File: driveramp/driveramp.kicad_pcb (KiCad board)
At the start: 4 copper layers, 17 parts, among them J1 SMA, J2 SMA, Q1 MRFE6VS25L

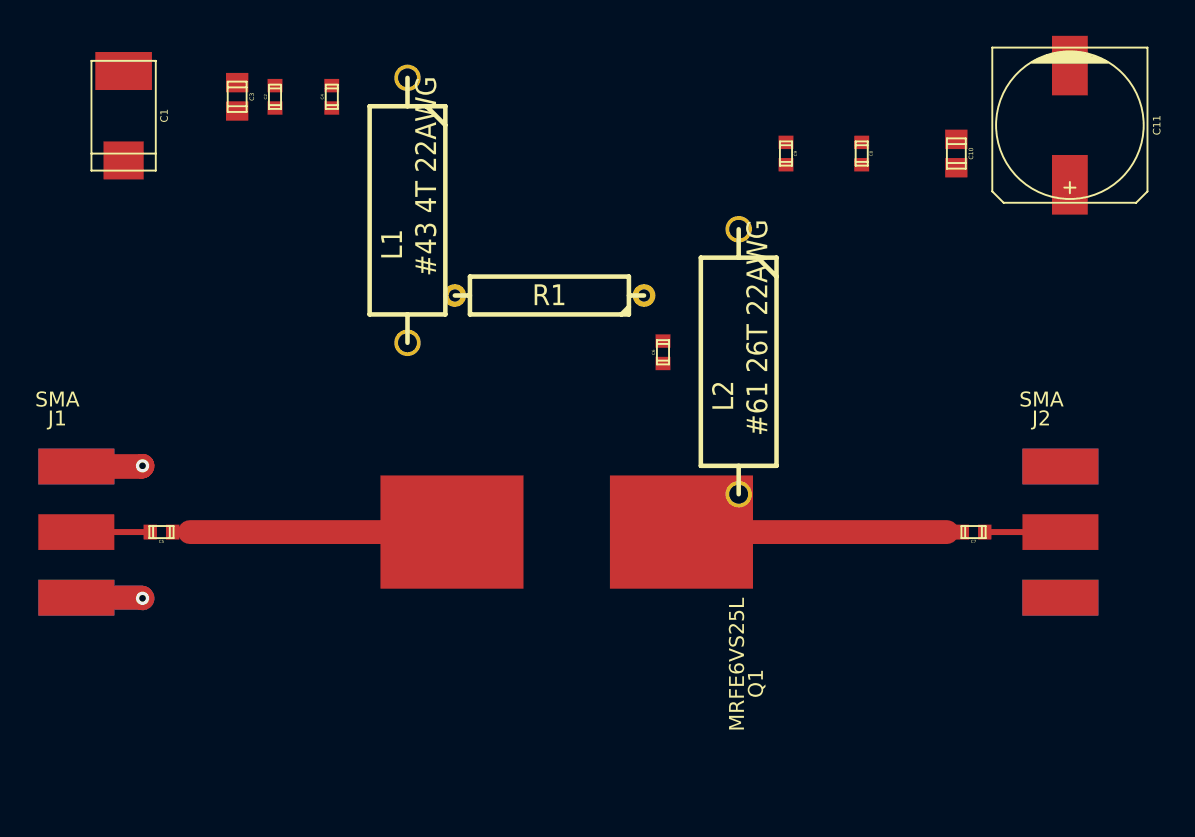
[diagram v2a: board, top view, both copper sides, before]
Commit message: layout work on driver amp
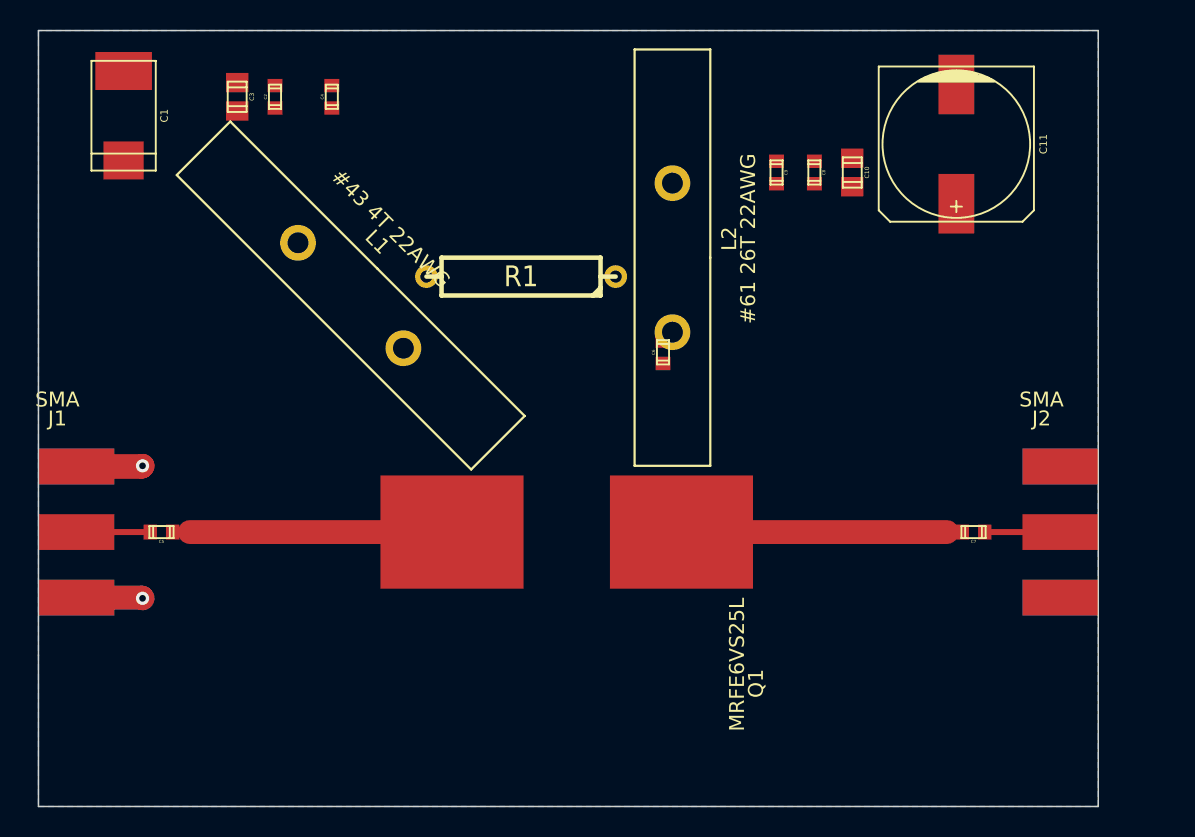
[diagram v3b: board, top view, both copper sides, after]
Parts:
- L1, L2: footprint R7 -> toroid
- moved L2 8.28 mm to (137.8, 63.5)
- moved C11 7.73 mm to (156.8, 55.9)
- moved C10 7.10 mm to (149.9, 57.8)
- moved L1 6.87 mm to (116.2, 66.0), turned to 315 degrees
- moved C8 3.42 mm to (147.3, 57.8)
- moved R1 2.29 mm to (127.6, 64.8)
- moved C9 1.42 mm to (144.8, 57.8)
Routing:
- added copper zone on B.Cu, net GND
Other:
- board outline added: 71.1 x 52.1 mm
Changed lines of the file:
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@@
   (general
     (links 32)
-    (no_connects 25)
-    (area 90.13962 30.966827 175.86188 97.235555)
+    (no_connects 23)
+    (area 93.978334 47.476827 171.41688 100.380001)
     (thickness 1.6)
-    (drawings 0)
+    (drawings 5)
     (tracks 17)
     (zones 0)
@@
     (2 Inner2.Cu power)
     (1 Inner1.Cu power)
-    (0 B.Cu signal)
+    (0 B.Cu signal hide)
     (16 B.Adhes user)
     (17 F.Adhes user)
@@
   )
   (setup
-    (last_trace_width 0.4)
+    (last_trace_width 0.254)
     (user_trace_width 0.254)
     (user_trace_width 0.4)
@@
     (mod_text_size 1 1)
     (mod_text_width 0.15)
-    (pad_size 5 2.4)
-    (pad_drill 0)
+    (pad_size 2.4 2.4)
+    (pad_drill 1.4)
     (pad_to_mask_clearance 0)
     (aux_axis_origin 0 0)
@@
     )
   )
-  (module R7 (layer F.Cu)
-    (at 120.015 60.325 270)
-    (descr "Resitance 7 pas")
-    (tags R)
-    (autoplace_cost180 10)
-    (fp_text reference L1 (at 2.286 1.016 270) (layer F.SilkS)
-      (effects (font (size 1.397 1.27) (thickness 0.2032)))
-    )
-    (fp_text value "#43 4T 22AWG" (at -2.286 -1.27 270) (layer F.SilkS)
-      (effects (font (size 1.397 1.27) (thickness 0.2032)))
-    )
-    (fp_line (start -8.89 0) (end -8.89 0) (layer F.SilkS) (width 0.3048))
-    (fp_line (start -8.89 0) (end -8.89 0) (layer F.SilkS) (width 0.3048))
-    (fp_line (start 6.985 0) (end 8.89 0) (layer F.SilkS) (width 0.3048))
-    (fp_line (start 8.89 0) (end 8.89 0) (layer F.SilkS) (width 0.3048))
-    (fp_line (start 6.985 2.54) (end -6.985 2.54) (layer F.SilkS) (width 0.3048))
-    (fp_line (start -6.985 -2.54) (end 6.985 -2.54) (layer F.SilkS) (width 0.3048))
-    (fp_line (start -6.985 -1.27) (end -5.715 -2.54) (layer F.SilkS) (width 0.3048))
-    (fp_line (start 6.985 -2.54) (end 6.985 2.54) (layer F.SilkS) (width 0.3048))
-    (fp_line (start -6.985 -2.54) (end -6.985 2.54) (layer F.SilkS) (width 0.3048))
-    (fp_line (start -8.89 0) (end -6.985 0) (layer F.SilkS) (width 0.3048))
-    (pad 1 thru_hole circle (at -8.89 0 270) (size 1.778 1.778) (drill 1.27)
-      (layers *.Cu *.Mask F.SilkS)
-      (net 1 /vbias)
-    )
-    (pad 2 thru_hole circle (at 8.89 0 270) (size 1.778 1.778) (drill 1.27)
-      (layers *.Cu *.Mask F.SilkS)
-      (net 6 N-000003)
-    )
-    (model discret/resistor.wrl
-      (at (xyz 0 0 0))
-      (scale (xyz 0.7 0.7 0.7))
-      (rotate (xyz 0 0 0))
-    )
-  )
-  (module R7 (layer F.Cu)
-    (at 142.24 70.485 270)
-    (descr "Resitance 7 pas")
-    (tags R)
-    (autoplace_cost180 10)
-    (fp_text reference L2 (at 2.286 1.016 270) (layer F.SilkS)
-      (effects (font (size 1.397 1.27) (thickness 0.2032)))
-    )
-    (fp_text value "#61 26T 22AWG" (at -2.286 -1.27 270) (layer F.SilkS)
-      (effects (font (size 1.397 1.27) (thickness 0.2032)))
-    )
-    (fp_line (start -8.89 0) (end -8.89 0) (layer F.SilkS) (width 0.3048))
-    (fp_line (start -8.89 0) (end -8.89 0) (layer F.SilkS) (width 0.3048))
-    (fp_line (start 6.985 0) (end 8.89 0) (layer F.SilkS) (width 0.3048))
-    (fp_line (start 8.89 0) (end 8.89 0) (layer F.SilkS) (width 0.3048))
-    (fp_line (start 6.985 2.54) (end -6.985 2.54) (layer F.SilkS) (width 0.3048))
-    (fp_line (start -6.985 -2.54) (end 6.985 -2.54) (layer F.SilkS) (width 0.3048))
-    (fp_line (start -6.985 -1.27) (end -5.715 -2.54) (layer F.SilkS) (width 0.3048))
-    (fp_line (start 6.985 -2.54) (end 6.985 2.54) (layer F.SilkS) (width 0.3048))
-    (fp_line (start -6.985 -2.54) (end -6.985 2.54) (layer F.SilkS) (width 0.3048))
-    (fp_line (start -8.89 0) (end -6.985 0) (layer F.SilkS) (width 0.3048))
-    (pad 1 thru_hole circle (at -8.89 0 270) (size 1.778 1.778) (drill 1.27)
-      (layers *.Cu *.Mask F.SilkS)
-      (net 2 /vsupply)
-    )
-    (pad 2 thru_hole circle (at 8.89 0 270) (size 1.778 1.778) (drill 1.27)
-      (layers *.Cu *.Mask F.SilkS)
-      (net 7 N-000007)
-    )
-    (model discret/resistor.wrl
-      (at (xyz 0 0 0))
-      (scale (xyz 0.7 0.7 0.7))
-      (rotate (xyz 0 0 0))
-    )
-  )
   (module R5 (layer F.Cu)
-    (at 129.54 66.04 180)
+    (at 127.635 64.77 180)
     (descr "Resistance 5 pas")
     (tags R)
@@
   )
   (module c_elec_10x10 (layer F.Cu)
-    (at 164.465 54.61 270)
+    (at 156.845 55.88 270)
     (descr "SMT capacitor, aluminium electrolytic, 10x10")
     (fp_text reference C11 (at 0 -5.842 270) (layer F.SilkS)
@@
   )
   (module c_0805 (layer F.Cu)
-    (at 156.845 56.515 270)
+    (at 149.86 57.785 270)
     (descr "SMT capacitor, 0805")
     (fp_text reference C10 (at 0 -0.9906 270) (layer F.SilkS)
@@
   )
   (module c_0603 (layer F.Cu)
-    (at 150.495 56.515 270)
+    (at 147.32 57.785 270)
     (descr "SMT capacitor, 0603")
     (fp_text reference C8 (at 0 -0.635 270) (layer F.SilkS)
@@
   )
   (module c_0603 (layer F.Cu)
-    (at 145.415 56.515 270)
+    (at 144.78 57.785 270)
     (descr "SMT capacitor, 0603")
     (fp_text reference C9 (at 0 -0.635 270) (layer F.SilkS)
@@
     )
   )
+  (module toroid (layer F.Cu)
+    (at 116.205 66.04 315)
+    (fp_text reference L1 (at -1.27 -3.81 315) (layer F.SilkS)
+      (effects (font (size 1 1) (thickness 0.15)))
+    )
+    (fp_text value "#43 4T 22AWG" (at -1.27 -5.08 315) (layer F.SilkS)
+      (effects (font (size 1 1) (thickness 0.15)))
+    )
+    (fp_line (start 0 -2.54) (end -13.97 -2.54) (layer F.SilkS) (width 0.15))
+    (fp_line (start -13.97 -2.54) (end -13.97 2.54) (layer F.SilkS) (width 0.15))
+    (fp_line (start -13.97 2.54) (end 13.97 2.54) (layer F.SilkS) (width 0.15))
+    (fp_line (start 13.97 2.54) (end 13.97 -2.54) (layer F.SilkS) (width 0.15))
+    (fp_line (start 13.97 -2.54) (end 0 -2.54) (layer F.SilkS) (width 0.15))
+    (pad 2 thru_hole circle (at 5 0 315) (size 2.4 2.4) (drill 1.4)
+      (layers *.Cu *.Mask F.SilkS)
+      (net 6 N-000003)
+    )
+    (pad 1 thru_hole circle (at -5 0 315) (size 2.4 2.4) (drill 1.4)
+      (layers *.Cu *.Mask F.SilkS)
+      (net 1 /vbias)
+    )
+  )
+  (module toroid (layer F.Cu)
+    (at 137.795 63.5 270)
+    (fp_text reference L2 (at -1.27 -3.81 270) (layer F.SilkS)
+      (effects (font (size 1 1) (thickness 0.15)))
+    )
+    (fp_text value "#61 26T 22AWG" (at -1.27 -5.08 270) (layer F.SilkS)
+      (effects (font (size 1 1) (thickness 0.15)))
+    )
+    (fp_line (start 0 -2.54) (end -13.97 -2.54) (layer F.SilkS) (width 0.15))
+    (fp_line (start -13.97 -2.54) (end -13.97 2.54) (layer F.SilkS) (width 0.15))
+    (fp_line (start -13.97 2.54) (end 13.97 2.54) (layer F.SilkS) (width 0.15))
+    (fp_line (start 13.97 2.54) (end 13.97 -2.54) (layer F.SilkS) (width 0.15))
+    (fp_line (start 13.97 -2.54) (end 0 -2.54) (layer F.SilkS) (width 0.15))
+    (pad 2 thru_hole circle (at 5 0 270) (size 2.4 2.4) (drill 1.4)
+      (layers *.Cu *.Mask F.SilkS)
+      (net 7 N-000007)
+    )
+    (pad 1 thru_hole circle (at -5 0 270) (size 2.4 2.4) (drill 1.4)
+      (layers *.Cu *.Mask F.SilkS)
+      (net 2 /vsupply)
+    )
+  )
+  (gr_line (start 95.25 48.26) (end 166.37 48.26) (angle 90) (layer Edge.Cuts) (width 0.1))
+  (gr_line (start 166.37 100.33) (end 166.37 48.26) (angle 90) (layer Edge.Cuts) (width 0.1))
+  (gr_line (start 95.25 100.33) (end 166.37 100.33) (angle 90) (layer Edge.Cuts) (width 0.1))
+  (gr_line (start 95.25 90.17) (end 95.25 100.33) (angle 90) (layer Edge.Cuts) (width 0.1))
+  (gr_line (start 95.25 90.17) (end 95.25 48.26) (angle 90) (layer Edge.Cuts) (width 0.1))
   (segment (start 97.79 77.515) (end 102.19 77.515) (width 1.6) (layer B.Cu) (net 3))
   (segment (start 97.79 77.515) (end 102.19 77.515) (width 1.6) (layer F.Cu) (net 3))
@@
   (segment (start 104.25684 81.915) (end 105.41 81.915) (width 0.4) (layer F.Cu) (net 8))
   (segment (start 105.41 81.915) (end 123 81.915) (width 1.6) (layer F.Cu) (net 8))
+  (zone (net 3) (net_name GND) (layer B.Cu) (hatch edge 0.508)
+    (connect_pads (clearance 0.508))
+    (min_thickness 0.254)
+    (fill (arc_segments 16) (thermal_gap 0.508) (thermal_bridge_width 0.508))
+    (polygon
+      (pts
+        (xy 95.25 48.26) (xy 95.25 100.33) (xy 166.37 100.33) (xy 166.37 48.26)
+      )
+    )
+  )
 )

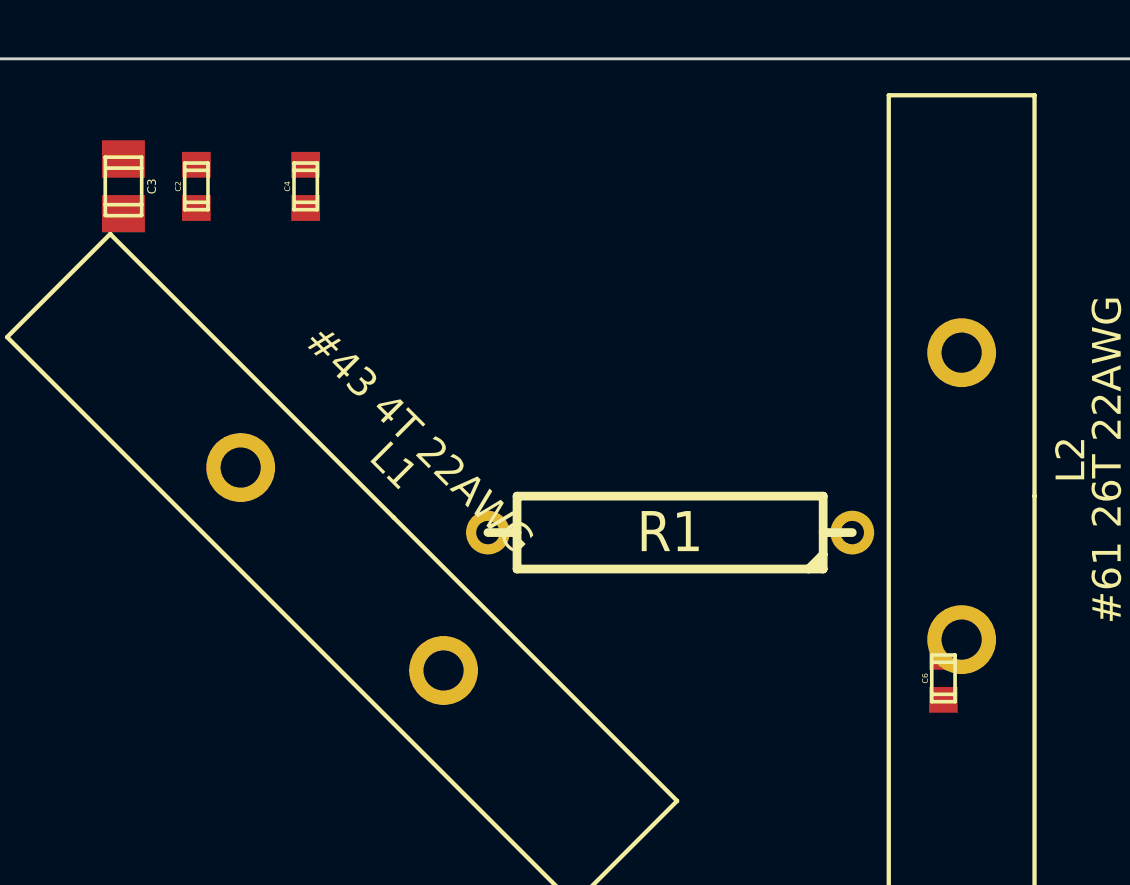
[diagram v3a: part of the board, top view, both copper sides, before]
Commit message: driver amp layout
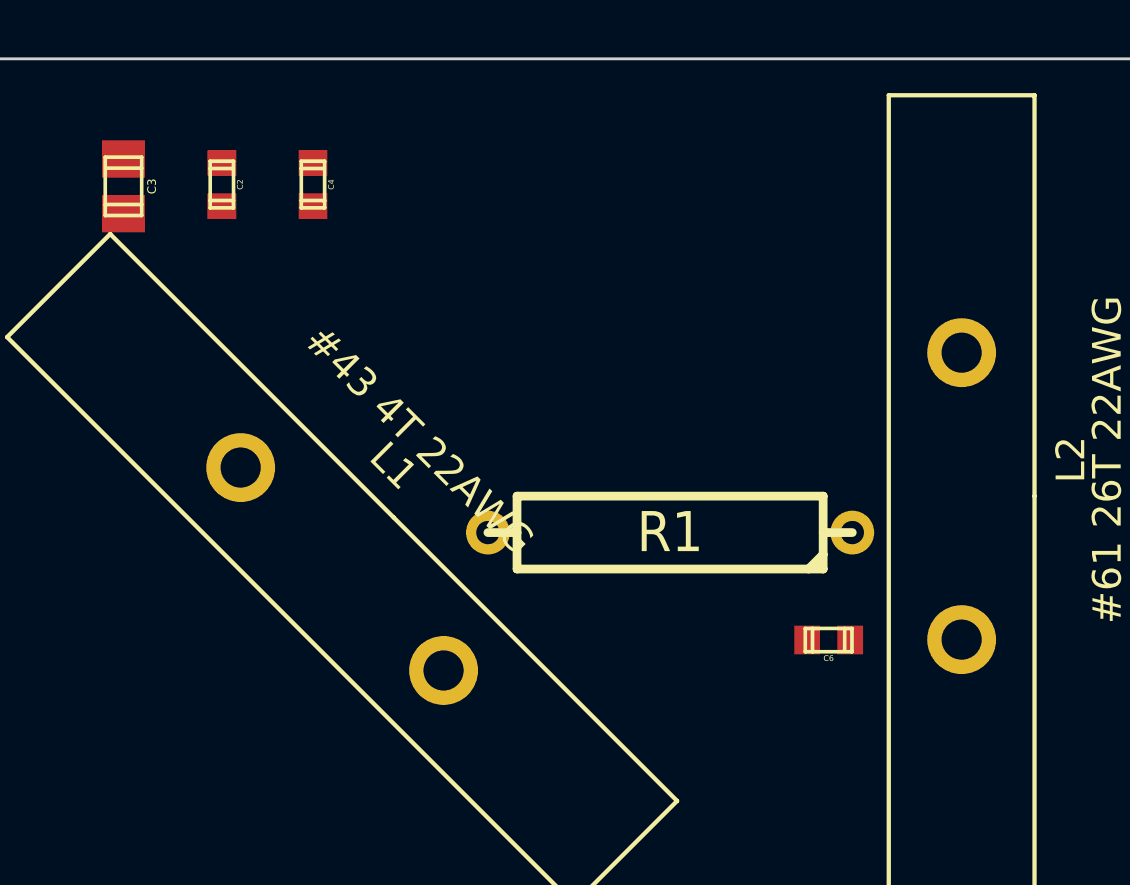
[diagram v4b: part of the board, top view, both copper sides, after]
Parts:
- moved C6 4.22 mm to (133.2, 68.5), turned to 180 degrees
- moved C2 0.89 mm to (112.0, 52.6), turned to 270 degrees
- moved C4 0.26 mm to (115.2, 52.6), turned to 270 degrees
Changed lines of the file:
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@@
     (links 32)
     (no_connects 23)
-    (area 93.978334 47.476827 171.41688 100.380001)
+    (area 93.978334 47.887133 167.448245 100.380001)
     (thickness 1.6)
     (drawings 5)
@@
   )
   (module c_0603 (layer F.Cu)
-    (at 111.125 52.705 90)
+    (at 112.014 52.6415 270)
     (descr "SMT capacitor, 0603")
-    (fp_text reference C2 (at 0 -0.635 90) (layer F.SilkS)
-      (effects (font (size 0.20066 0.20066) (thickness 0.04064)))
-    )
-    (fp_text value "100nF 50V" (at 0 0.635 90) (layer F.SilkS) hide
+    (fp_text reference C2 (at 0 -0.635 270) (layer F.SilkS)
+      (effects (font (size 0.20066 0.20066) (thickness 0.04064)))
+    )
+    (fp_text value "100nF 50V" (at 0 0.635 270) (layer F.SilkS) hide
       (effects (font (size 0.20066 0.20066) (thickness 0.04064)))
     )
@@
     (fp_line (start 0.8128 0.4064) (end -0.8128 0.4064) (layer F.SilkS) (width 0.127))
     (fp_line (start -0.8128 0.4064) (end -0.8128 -0.4064) (layer F.SilkS) (width 0.127))
-    (pad 1 smd rect (at 0.75184 0 90) (size 0.89916 1.00076)
+    (pad 1 smd rect (at 0.75184 0 270) (size 0.89916 1.00076)
       (layers F.Cu F.Paste F.Mask)
       (net 1 /vbias)
     )
-    (pad 2 smd rect (at -0.75184 0 90) (size 0.89916 1.00076)
+    (pad 2 smd rect (at -0.75184 0 270) (size 0.89916 1.00076)
       (layers F.Cu F.Paste F.Mask)
       (net 3 GND)
@@
   )
   (module c_0603 (layer F.Cu)
-    (at 114.935 52.705 90)
+    (at 115.189 52.6415 270)
     (descr "SMT capacitor, 0603")
-    (fp_text reference C4 (at 0 -0.635 90) (layer F.SilkS)
-      (effects (font (size 0.20066 0.20066) (thickness 0.04064)))
-    )
-    (fp_text value 10nF (at 0 0.635 90) (layer F.SilkS) hide
+    (fp_text reference C4 (at 0 -0.635 270) (layer F.SilkS)
+      (effects (font (size 0.20066 0.20066) (thickness 0.04064)))
+    )
+    (fp_text value 10nF (at 0 0.635 270) (layer F.SilkS) hide
       (effects (font (size 0.20066 0.20066) (thickness 0.04064)))
     )
@@
     (fp_line (start 0.8128 0.4064) (end -0.8128 0.4064) (layer F.SilkS) (width 0.127))
     (fp_line (start -0.8128 0.4064) (end -0.8128 -0.4064) (layer F.SilkS) (width 0.127))
-    (pad 1 smd rect (at 0.75184 0 90) (size 0.89916 1.00076)
+    (pad 1 smd rect (at 0.75184 0 270) (size 0.89916 1.00076)
       (layers F.Cu F.Paste F.Mask)
       (net 1 /vbias)
     )
-    (pad 2 smd rect (at -0.75184 0 90) (size 0.89916 1.00076)
+    (pad 2 smd rect (at -0.75184 0 270) (size 0.89916 1.00076)
       (layers F.Cu F.Paste F.Mask)
       (net 3 GND)
@@
   )
   (module c_0603 (layer F.Cu)
-    (at 137.16 69.85 90)
+    (at 133.1595 68.5165 180)
     (descr "SMT capacitor, 0603")
-    (fp_text reference C6 (at 0 -0.635 90) (layer F.SilkS)
-      (effects (font (size 0.20066 0.20066) (thickness 0.04064)))
-    )
-    (fp_text value 20nF (at 0 0.635 90) (layer F.SilkS) hide
+    (fp_text reference C6 (at 0 -0.635 180) (layer F.SilkS)
+      (effects (font (size 0.20066 0.20066) (thickness 0.04064)))
+    )
+    (fp_text value 20nF (at 0 0.635 180) (layer F.SilkS) hide
       (effects (font (size 0.20066 0.20066) (thickness 0.04064)))
     )
@@
     (fp_line (start 0.8128 0.4064) (end -0.8128 0.4064) (layer F.SilkS) (width 0.127))
     (fp_line (start -0.8128 0.4064) (end -0.8128 -0.4064) (layer F.SilkS) (width 0.127))
-    (pad 1 smd rect (at 0.75184 0 90) (size 0.89916 1.00076)
+    (pad 1 smd rect (at 0.75184 0 180) (size 0.89916 1.00076)
       (layers F.Cu F.Paste F.Mask)
       (net 9 N-000009)
     )
-    (pad 2 smd rect (at -0.75184 0 90) (size 0.89916 1.00076)
+    (pad 2 smd rect (at -0.75184 0 180) (size 0.89916 1.00076)
       (layers F.Cu F.Paste F.Mask)
       (net 7 N-000007)

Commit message: r0 driver amp breakout ready for manufacturing:
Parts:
- added P1: CONN_2, connect:SIL-2, F.Cu at (118.6, 51.8)
- added P2: CONN_2, connect:SIL-2, F.Cu at (145.3, 51.6)
- L1: value #43 4T 22AWG -> #43 4T 22AWG .01mH
- L2: value #61 26T 22AWG -> #61 26T 22AWG, .04mH
- moved L2 7.75 mm to (140.7, 70.7)
- moved C6 4.97 mm to (135.6, 72.9), turned to 90 degrees
- moved R1 3.39 mm to (129.2, 67.8)
- moved C4 2.48 mm to (113.3, 51.1)
- moved C3 1.94 mm to (109.0, 50.8)
- moved C2 1.76 mm to (111.3, 51.1)
- moved C1 1.20 mm to (99.8, 54.4), turned to 90 degrees
- moved L1 1.17 mm to (115.1, 65.8)
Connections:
- C5 pad 2: N-000008 -> Net-(C5-Pad2)
- L1 pad 2: N-000003 -> Net-(C5-Pad2)
- Q1 pad G: N-000008 -> Net-(C5-Pad2)
- R1 pad 2: N-000003 -> Net-(C5-Pad2)
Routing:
- net Net-(C5-Pad2): track 0.00 -> 38.0 mm
- net /vsupply: track 0.00 -> 37.5 mm
- net GND: track 22.3 -> 58.5 mm, vias 2 -> 12
- net /vbias: track 0.00 -> 32.8 mm
- net Net-(C6-Pad2): track 18.8 -> 39.4 mm
- net N-000008: track 18.7 -> 0.00 mm
- net Net-(C6-Pad1): track 0.00 -> 4.36 mm
- net Net-(C5-Pad1): track 4.96 -> 5.61 mm
- net Net-(C7-Pad2): track 5.08 -> 5.71 mm
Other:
- board text added: "jon klein jtklein@alaska.edu driver amp breakout"
- board text added: "this side down"
- board text added: "vbias"
- board text added: "vdd"

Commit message: added barrel connector to driver amp, finished medium power T/R layout
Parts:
- removed P1: CONN_2, connect:SIL-2
- added CON1: BARREL_JACK, connect:BARREL_JACK, F.Cu at (132.6, 52.3)
- added K1: CONN_3, connect:SIL-3, F.Cu at (118.0, 54.5)
- added RV1: POT, connect:SIL-3, F.Cu at (123.3, 54.5)
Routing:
- net GND: track 58.5 -> 66.3 mm
- net /vbias: track 32.8 -> 39.1 mm
- net Net-(K1-Pad1): track 0.00 -> 5.33 mm
